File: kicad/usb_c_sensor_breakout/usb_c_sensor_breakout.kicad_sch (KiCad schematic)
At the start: 0 parts

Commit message: commit2: usbc + regulator + i2c pullups + sensor header + testpoint
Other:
- added sheet CONNECTORS (CONNECTORS.kiCad_sch)
- added sheet POWER_INPUT (POWER_INPUT.kicad_sch)
- added sheet REGULATOR_3V3 (REGULATOR_3V3.kicad_sch)
- added sheet SENSOR_I2C (SENSOR_I2C.kicad_sch)
- company: (none) -> Personal Project
- title: (none) -> USB-C Sensor Breakout Board

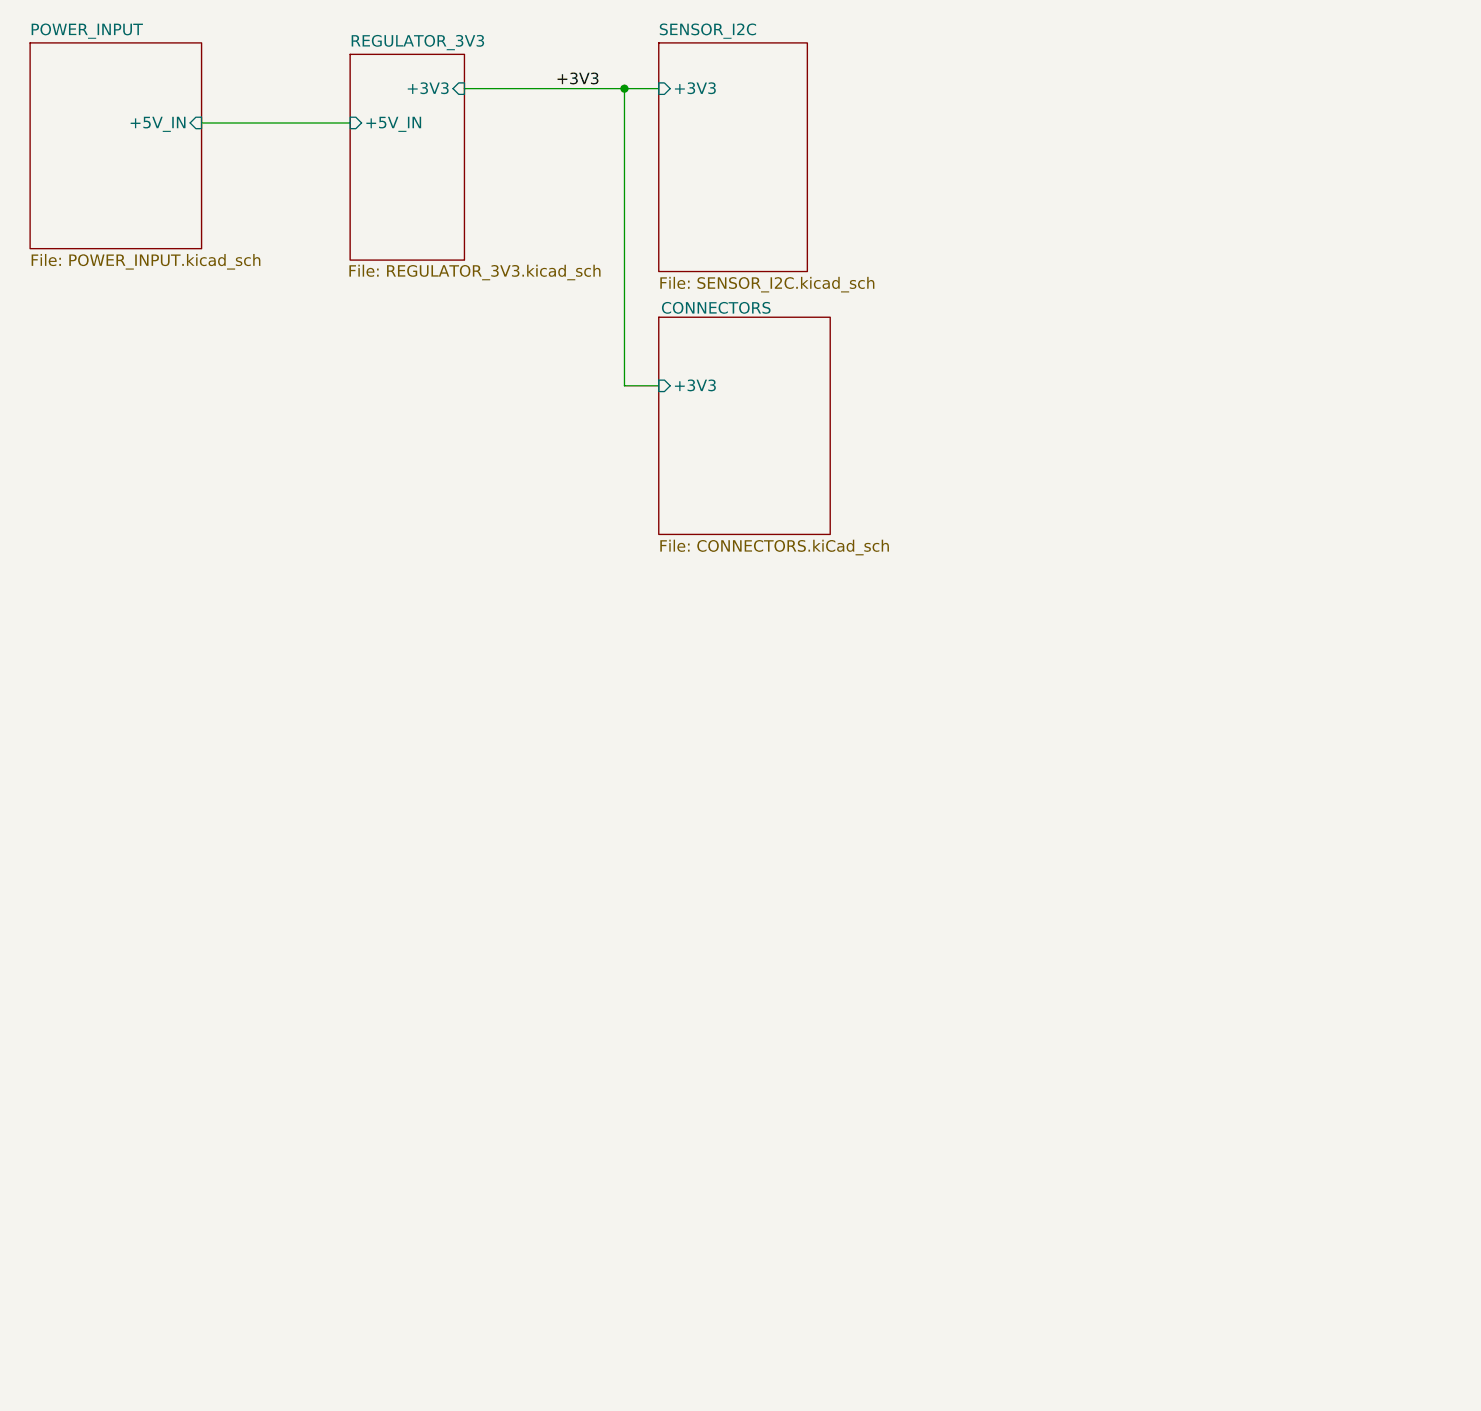
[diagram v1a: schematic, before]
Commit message: Commit3: Regulators + Top-level + I2C sensor upgrade
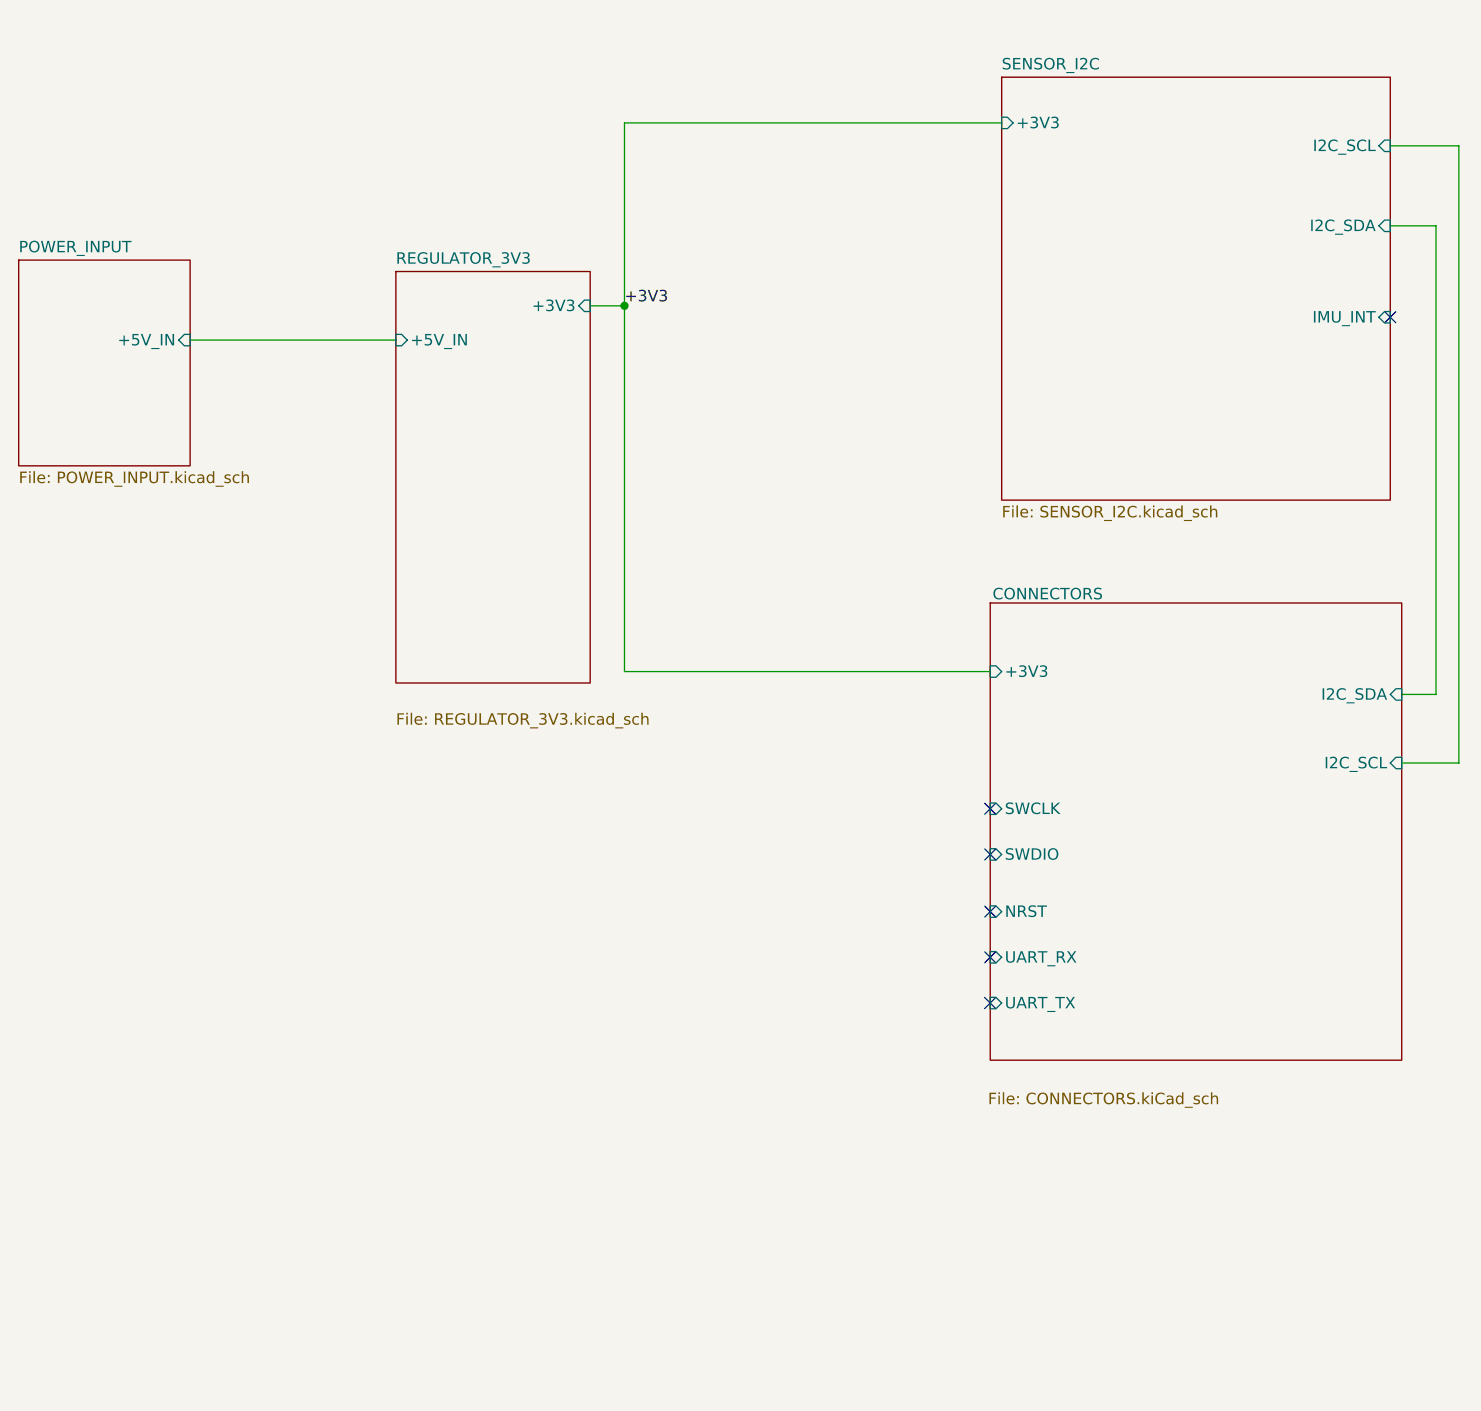
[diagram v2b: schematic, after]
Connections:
- no-connect marks 0 -> 6
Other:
- sheet CONNECTORS ports: added I2C_SCL, I2C_SDA, NRST, SWCLK, SWDIO, UART_RX, UART_TX; removed none
- sheet SENSOR_I2C ports: added I2C_SCL, I2C_SDA, IMU_INT; removed none
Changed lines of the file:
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@@
 	)
 	(junction
-		(at 87.63 25.4)
+		(at 87.63 49.53)
 		(diameter 0)
 		(color 0 0 0 0)
 	)
-	(wire
-		(pts
-			(xy 91.44 58.42) (xy 87.63 58.42)
-		)
-		(stroke
-			(width 0)
-			(type default)
-		)
-	)
-	(wire
-		(pts
-			(xy 87.63 25.4) (xy 91.44 25.4)
-		)
-		(stroke
-			(width 0)
-			(type default)
-		)
-	)
-	(wire
-		(pts
-			(xy 69.85 25.4) (xy 87.63 25.4)
-		)
-		(stroke
-			(width 0)
-			(type default)
-		)
-	)
-	(wire
-		(pts
-			(xy 40.64 29.21) (xy 57.15 29.21)
-		)
-		(stroke
-			(width 0)
-			(type default)
-		)
-	)
-	(wire
-		(pts
-			(xy 87.63 58.42) (xy 87.63 25.4)
+	(no_connect
+		(at 128.27 121.92)
+	)
+	(no_connect
+		(at 128.27 116.84)
+	)
+	(no_connect
+		(at 128.27 105.41)
+	)
+	(no_connect
+		(at 128.27 127)
+	)
+	(no_connect
+		(at 172.72 50.8)
+	)
+	(no_connect
+		(at 128.27 110.49)
+	)
+	(wire
+		(pts
+			(xy 128.27 90.17) (xy 87.63 90.17)
+		)
+		(stroke
+			(width 0)
+			(type default)
+		)
+	)
+	(wire
+		(pts
+			(xy 87.63 49.53) (xy 87.63 90.17)
+		)
+		(stroke
+			(width 0)
+			(type default)
+		)
+	)
+	(wire
+		(pts
+			(xy 177.8 92.71) (xy 173.99 92.71)
+		)
+		(stroke
+			(width 0)
+			(type default)
+		)
+	)
+	(wire
+		(pts
+			(xy 39.37 53.34) (xy 62.23 53.34)
+		)
+		(stroke
+			(width 0)
+			(type default)
+		)
+	)
+	(wire
+		(pts
+			(xy 172.72 31.75) (xy 180.34 31.75)
+		)
+		(stroke
+			(width 0)
+			(type default)
+		)
+	)
+	(wire
+		(pts
+			(xy 177.8 40.64) (xy 177.8 92.71)
+		)
+		(stroke
+			(width 0)
+			(type default)
+		)
+	)
+	(wire
+		(pts
+			(xy 180.34 31.75) (xy 180.34 100.33)
+		)
+		(stroke
+			(width 0)
+			(type default)
+		)
+	)
+	(wire
+		(pts
+			(xy 87.63 29.21) (xy 129.54 29.21)
+		)
+		(stroke
+			(width 0)
+			(type default)
+		)
+	)
+	(wire
+		(pts
+			(xy 172.72 40.64) (xy 177.8 40.64)
+		)
+		(stroke
+			(width 0)
+			(type default)
+		)
+	)
+	(wire
+		(pts
+			(xy 83.82 49.53) (xy 87.63 49.53)
+		)
+		(stroke
+			(width 0)
+			(type default)
+		)
+	)
+	(wire
+		(pts
+			(xy 180.34 100.33) (xy 173.99 100.33)
+		)
+		(stroke
+			(width 0)
+			(type default)
+		)
+	)
+	(wire
+		(pts
+			(xy 87.63 49.53) (xy 87.63 29.21)
 		)
 		(stroke
@@
 	)
 	(label "+3V3"
-		(at 80.01 25.4 0)
+		(at 87.63 49.53 0)
 		(effects
 			(font
@@
 	)
 	(sheet
-		(at 21.59 20.32)
+		(at 20.32 44.45)
 		(size 19.05 22.86)
 		(exclude_from_sim no)
@@
 		)
 		(property "Sheetname" "POWER_INPUT"
-			(at 21.59 19.6084 0)
+			(at 20.32 43.7384 0)
 			(effects
 				(font
@@
 		)
 		(property "Sheetfile" "POWER_INPUT.kicad_sch"
-			(at 21.59 43.7646 0)
+			(at 20.32 67.8946 0)
 			(effects
 				(font
@@
 		)
 		(pin "+5V_IN" input
-			(at 40.64 29.21 0)
+			(at 39.37 53.34 0)
 			(effects
 				(font
@@
 	)
 	(sheet
-		(at 57.15 21.59)
-		(size 12.7 22.86)
+		(at 62.23 45.72)
+		(size 21.59 45.72)
 		(exclude_from_sim no)
 		(in_bom yes)
@@
 		)
 		(property "Sheetname" "REGULATOR_3V3"
-			(at 57.15 20.8784 0)
+			(at 62.23 45.0084 0)
 			(effects
 				(font
@@
 		)
 		(property "Sheetfile" "REGULATOR_3V3.kicad_sch"
-			(at 56.896 44.958 0)
+			(at 62.23 94.742 0)
 			(effects
 				(font
@@
 		)
 		(pin "+3V3" input
-			(at 69.85 25.4 0)
+			(at 83.82 49.53 0)
 			(effects
 				(font
@@
 		)
 		(pin "+5V_IN" input
-			(at 57.15 29.21 180)
+			(at 62.23 53.34 180)
 			(effects
 				(font
@@
 	)
 	(sheet
-		(at 91.44 50.8)
-		(size 19.05 24.13)
+		(at 128.27 82.55)
+		(size 45.72 50.8)
 		(exclude_from_sim no)
 		(in_bom yes)
@@
 		)
 		(property "Sheetname" "CONNECTORS"
-			(at 91.694 50.546 0)
+			(at 128.524 82.296 0)
 			(effects
 				(font
@@
 		)
 		(property "Sheetfile" "CONNECTORS.kiCad_sch"
-			(at 91.44 75.5146 0)
+			(at 128.016 136.906 0)
 			(effects
 				(font
@@
 		)
 		(pin "+3V3" input
-			(at 91.44 58.42 180)
+			(at 128.27 90.17 180)
+			(effects
+				(font
+					(size 1.27 1.27)
+				)
+				(justify left)
+			)
+		)
+		(pin "I2C_SDA" input
+			(at 173.99 92.71 0)
+			(effects
+				(font
+					(size 1.27 1.27)
+				)
+				(justify right)
+			)
+		)
+		(pin "I2C_SCL" input
+			(at 173.99 100.33 0)
+			(effects
+				(font
+					(size 1.27 1.27)
+				)
+				(justify right)
+			)
+		)
+		(pin "SWCLK" input
+			(at 128.27 105.41 180)
+			(effects
+				(font
+					(size 1.27 1.27)
+				)
+				(justify left)
+			)
+		)
+		(pin "SWDIO" input
+			(at 128.27 110.49 180)
+			(effects
+				(font
+					(size 1.27 1.27)
+				)
+				(justify left)
+			)
+		)
+		(pin "NRST" input
+			(at 128.27 116.84 180)
+			(effects
+				(font
+					(size 1.27 1.27)
+				)
+				(justify left)
+			)
+		)
+		(pin "UART_RX" input
+			(at 128.27 121.92 180)
+			(effects
+				(font
+					(size 1.27 1.27)
+				)
+				(justify left)
+			)
+		)
+		(pin "UART_TX" input
+			(at 128.27 127 180)
 			(effects
 				(font
@@
 	)
 	(sheet
-		(at 91.44 20.32)
-		(size 16.51 25.4)
+		(at 129.54 24.13)
+		(size 43.18 46.99)
 		(exclude_from_sim no)
 		(in_bom yes)
@@
 		)
 		(property "Sheetname" "SENSOR_I2C"
-			(at 91.44 19.6084 0)
+			(at 129.54 23.4184 0)
 			(effects
 				(font
@@
 		)
 		(property "Sheetfile" "SENSOR_I2C.kicad_sch"
-			(at 91.44 46.3046 0)
+			(at 129.54 71.7046 0)
 			(effects
 				(font
@@
 		)
 		(pin "+3V3" input
-			(at 91.44 25.4 180)
-			(effects
-				(font
-					(size 1.27 1.27)
-				)
-				(justify left)
-			)
-		)
+			(at 129.54 29.21 180)
+			(effects
+				(font
+					(size 1.27 1.27)
+				)
+				(justify left)
+			)
+		)
+		(pin "I2C_SCL" input
+			(at 172.72 31.75 0)
+			(effects
+				(font
+					(size 1.27 1.27)
+				)
+				(justify right)
+			)
+		)
+		(pin "I2C_SDA" input
+			(at 172.72 40.64 0)
+			(effects
+				(font
+					(size 1.27 1.27)
+				)
+				(justify right)
+			)
+		)
+		(pin "IMU_INT" input
+			(at 172.72 50.8 0)
+			(effects
+				(font
+					(size 1.27 1.27)
+				)
+				(justify right)
+			)
+		)

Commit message: Commit 5: MCU + Final Schematic Touches + Labelling + USBc fix
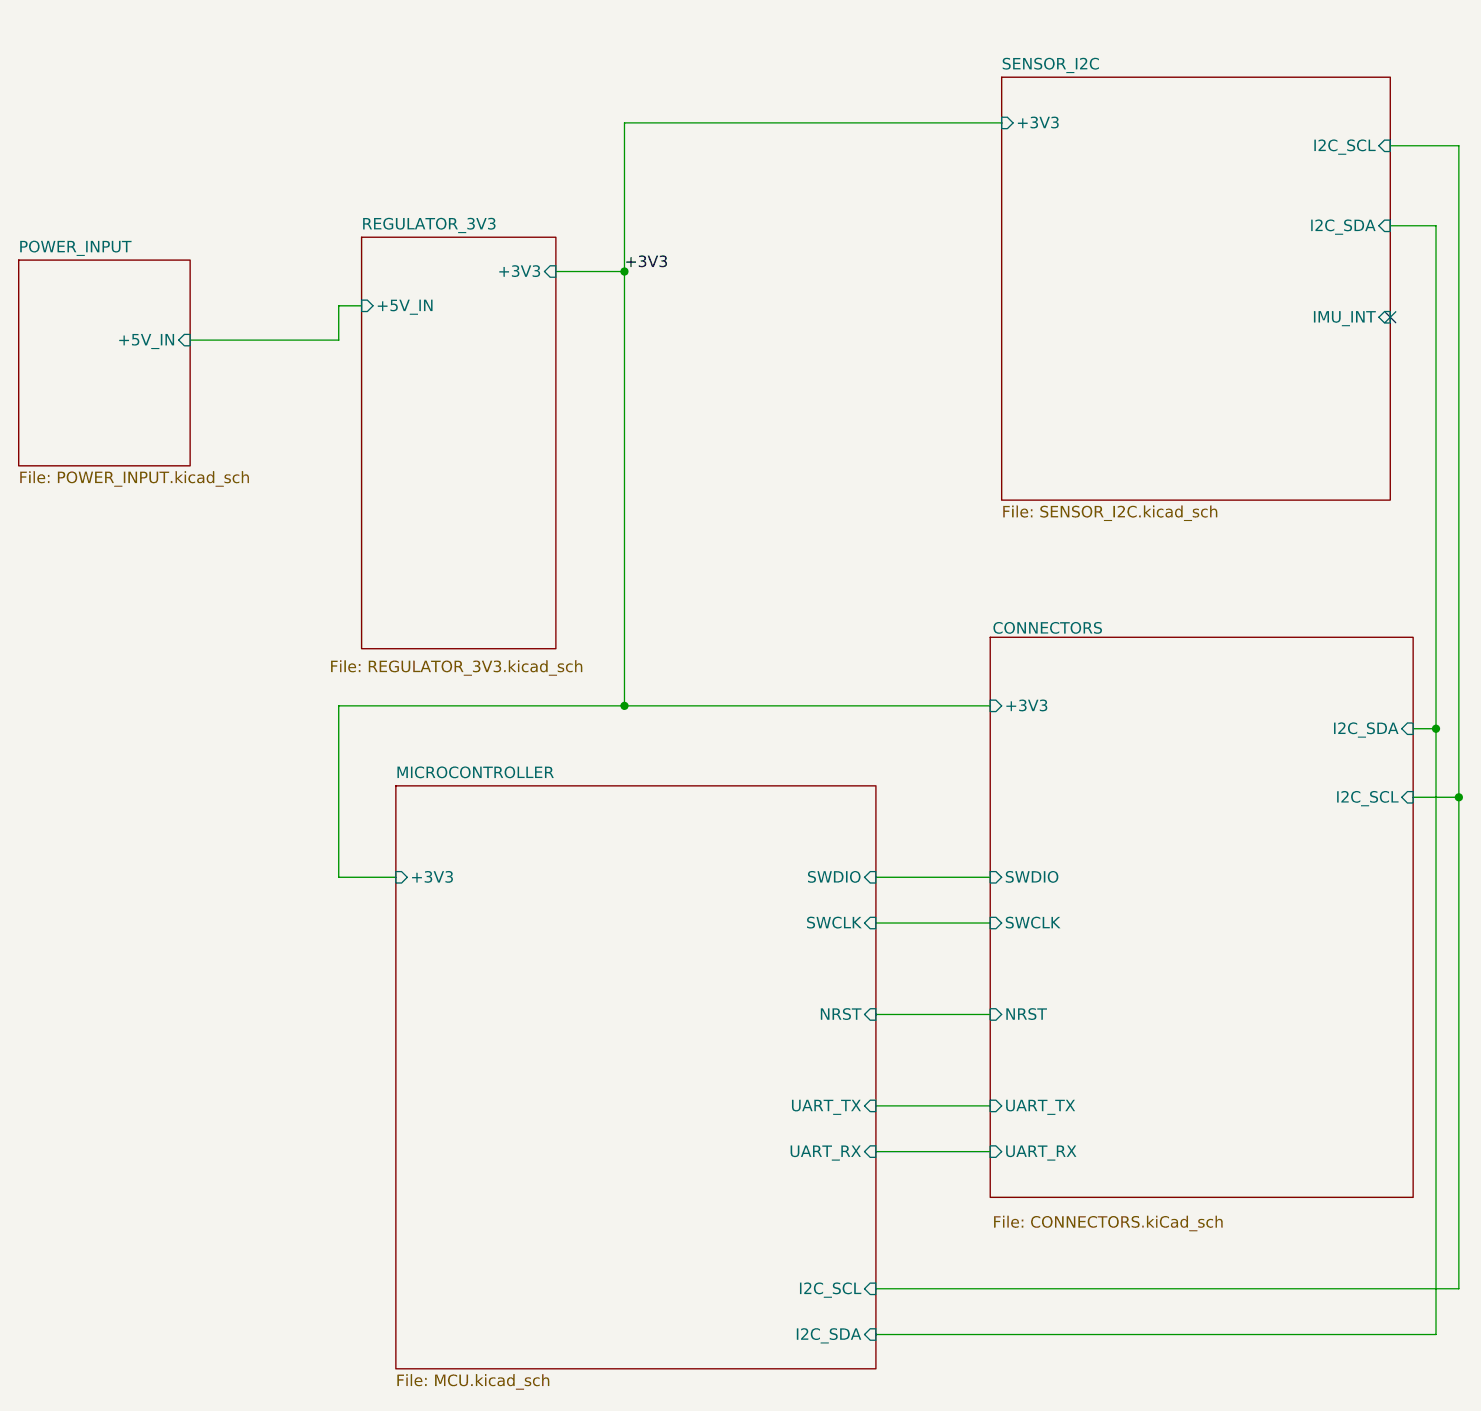
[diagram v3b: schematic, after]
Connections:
- no-connect marks 6 -> 1
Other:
- added sheet MICROCONTROLLER (MCU.kicad_sch)

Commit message: Commit 6: Finished PCB + Updated Schematic
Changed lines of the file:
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@@
-	(wire
-		(pts
-			(xy 55.88 53.34) (xy 55.88 49.53)
-		)
-		(stroke
-			(width 0)
-			(type default)
-		)
-	)
 	(wire
 		(pts
@@
 	(wire
 		(pts
-			(xy 39.37 53.34) (xy 55.88 53.34)
+			(xy 40.64 49.53) (xy 58.42 49.53)
 		)
 		(stroke
@@
 		(pts
 			(xy 87.63 93.98) (xy 55.88 93.98)
-		)
-		(stroke
-			(width 0)
-			(type default)
-		)
-	)
-	(wire
-		(pts
-			(xy 55.88 49.53) (xy 58.42 49.53)
 		)
 		(stroke
@@
 	)
 	(sheet
-		(at 20.32 44.45)
+		(at 21.59 40.64)
 		(size 19.05 22.86)
 		(exclude_from_sim no)
@@
 		)
 		(property "Sheetname" "POWER_INPUT"
-			(at 20.32 43.7384 0)
+			(at 21.59 39.9284 0)
 			(effects
 				(font
@@
 		)
 		(property "Sheetfile" "POWER_INPUT.kicad_sch"
-			(at 20.32 67.8946 0)
+			(at 21.59 64.0846 0)
 			(effects
 				(font
@@
 			)
 		)
-		(pin "+5V_IN" input
-			(at 39.37 53.34 0)
+		(pin "+5V_IN" output
+			(at 40.64 49.53 0)
 			(effects
 				(font
@@
 			)
 		)
-		(pin "+3V3" input
+		(pin "+3V3" output
 			(at 80.01 45.72 0)
 			(effects
@@
 			)
 		)
-		(pin "I2C_SDA" input
+		(pin "I2C_SDA" bidirectional
 			(at 175.26 96.52 0)
 			(effects
@@
 			)
 		)
-		(pin "I2C_SCL" input
+		(pin "I2C_SCL" bidirectional
 			(at 175.26 104.14 0)
 			(effects
@@
 			)
 		)
-		(pin "SWDIO" input
+		(pin "SWDIO" bidirectional
 			(at 128.27 113.03 180)
 			(effects
@@
 			)
 		)
-		(pin "NRST" input
+		(pin "NRST" bidirectional
 			(at 128.27 128.27 180)
 			(effects
@@
 			)
 		)
-		(pin "UART_TX" input
+		(pin "UART_TX" output
 			(at 128.27 138.43 180)
 			(effects
@@
 			)
 		)
-		(pin "I2C_SCL" input
+		(pin "I2C_SCL" bidirectional
 			(at 115.57 158.75 0)
 			(effects
@@
 			)
 		)
-		(pin "I2C_SDA" input
+		(pin "I2C_SDA" bidirectional
 			(at 115.57 163.83 0)
 			(effects
@@
 			)
 		)
-		(pin "SWCLK" input
+		(pin "SWCLK" output
 			(at 115.57 118.11 0)
 			(effects
@@
 			)
 		)
-		(pin "SWDIO" input
+		(pin "SWDIO" bidirectional
 			(at 115.57 113.03 0)
 			(effects
@@
 			)
 		)
-		(pin "UART_TX" input
+		(pin "UART_TX" output
 			(at 115.57 138.43 0)
 			(effects
@@
 			)
 		)
-		(pin "I2C_SDA" input
+		(pin "I2C_SDA" bidirectional
 			(at 172.72 40.64 0)
 			(effects
@@
 			)
 		)
-		(pin "IMU_INT" input
+		(pin "IMU_INT" output
 			(at 172.72 50.8 0)
 			(effects
